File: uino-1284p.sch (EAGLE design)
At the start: 61 parts, among them J1 Micro USB, J2 M03X2, J3 CON_TERMINAL_BLOCK_02-5MM, J4 M03X2, J5 IO, Q1 MMBF0202PLT1, U1 ATMEGA8U2AU, U2 LD117AS50TR, U3 ATMEGA1284AU, X1 16MHz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

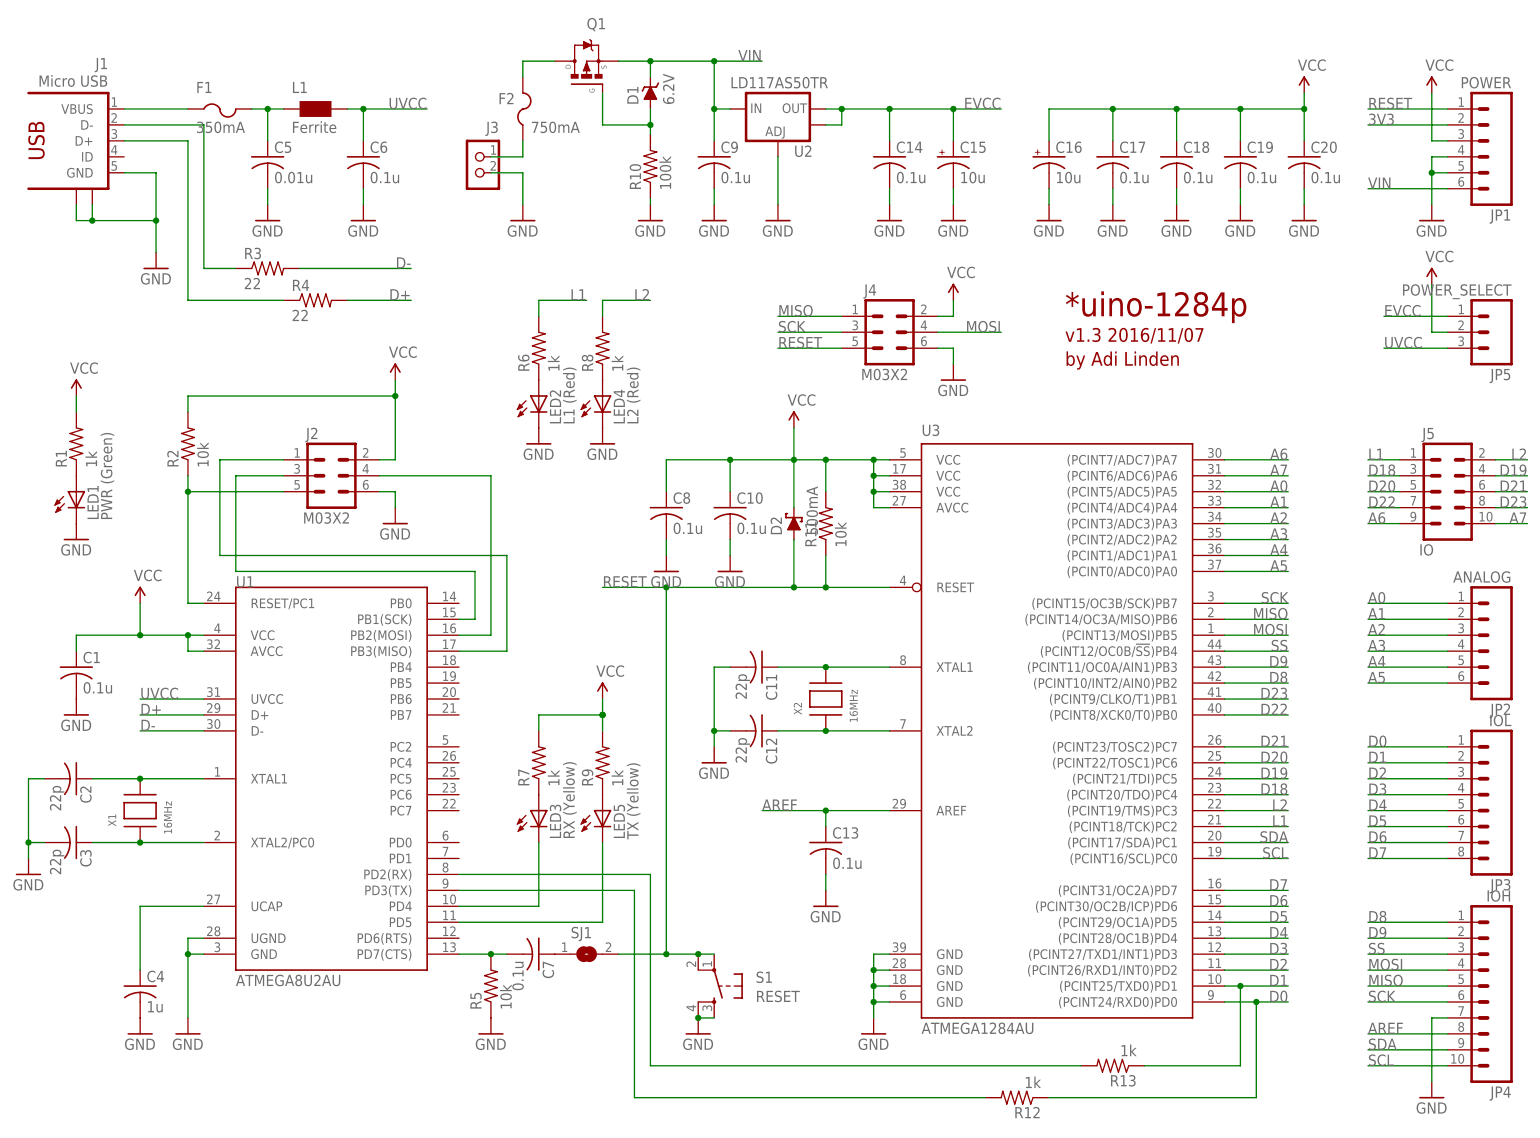
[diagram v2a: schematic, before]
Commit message: Changed tantalum to 0805 and ceramic.  Made use of extra space.
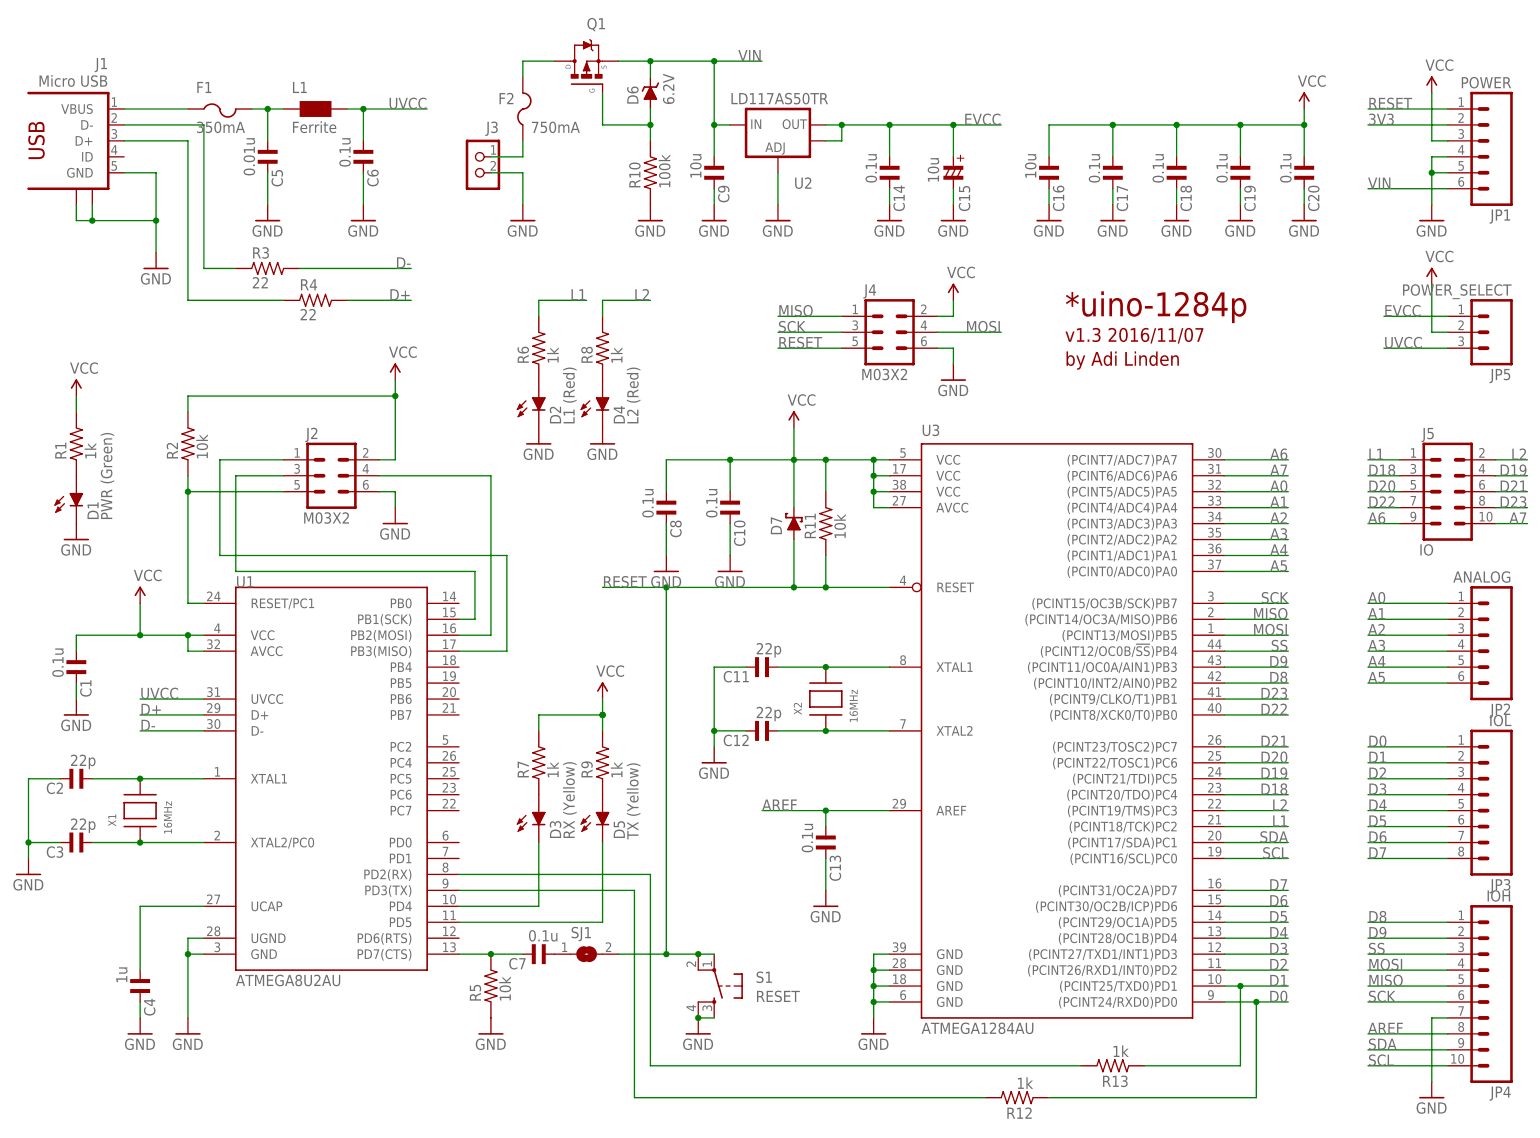
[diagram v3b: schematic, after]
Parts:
- removed LED1: PWR (Green), adafruit:LEDCHIP-LED0805
- removed LED2: L1 (Red), adafruit:LEDCHIP-LED0805
- removed LED3: RX (Yellow), adafruit:LEDCHIP-LED0805
- removed LED4: L2 (Red), adafruit:LEDCHIP-LED0805
- removed LED5: TX (Yellow), adafruit:LEDCHIP-LED0805
- added D3: RX (Yellow), led:LEDCHIP-LED0805MP
- added D4: L2 (Red), led:LEDCHIP-LED0805MP
- added D5: TX (Yellow), led:LEDCHIP-LED0805MP
- added D6: 6.2V, diode:BZX384
- added D7: (no value), diode:SCHOTTKY-DIODESOD323
- C1, C10, C11, C12, C13, C14, C17, C18, C19, C2, C20, C3, C4, C5, C6, C7, C8: device rcl:C-USC0805 -> rc-master-smd:C_0805MP
- C15: device rcl:CPOL-USCT3216 -> rc-master-smd:CP_0805MP/T
- C16: device rcl:CPOL-USCT3216 -> rc-master-smd:C_0805MP
- C9: value 0.1u -> 10u; device rcl:C-USC0805 -> rc-master-smd:C_0805MP
- D1: value 6.2V -> PWR (Green); device diode:BZX384 -> led:LEDCHIP-LED0805MP
- D2: value 500mA -> L1 (Red); device diode:SCHOTTKY-DIODESOD323 -> led:LEDCHIP-LED0805MP
- R1, R10, R11, R12, R13, R2, R3, R4, R5, R6, R7, R8, R9: device rcl:R-US_R0805 -> rc-master-smd:R_0805MP
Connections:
- net GND: now also C16.2, D1.C, D2.C, D4.C; no longer C16.-, LED1.C, LED2.C, LED4.C
- net N$11: now also D2.A; no longer LED2.A
- net N$12: now also D4.A; no longer LED4.A
- net N$18: now also D6.A; no longer D1.A
- net N$26: now also D3.A; no longer LED3.A
- net N$27: now also D5.A; no longer LED5.A
- net N$29: now also D3.C; no longer LED3.C
- net N$30: now also D5.C; no longer LED5.C
- net N$34: now also D1.A; no longer LED1.A
- net RESET: now also D7.A; no longer D2.A
- net VCC: now also C16.1, D7.C; no longer C16.+, D2.C
- net VIN: now also D6.C; no longer D1.C
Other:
- moved on the sheet: C15, D2, R10, U2
